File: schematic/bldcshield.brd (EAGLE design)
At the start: 90.2 x 53.3 mm, 51 parts, among them IC1 IR2101SMD, IC2 IR2101SMD, IC3 IR2101SMD, Q3 Shield

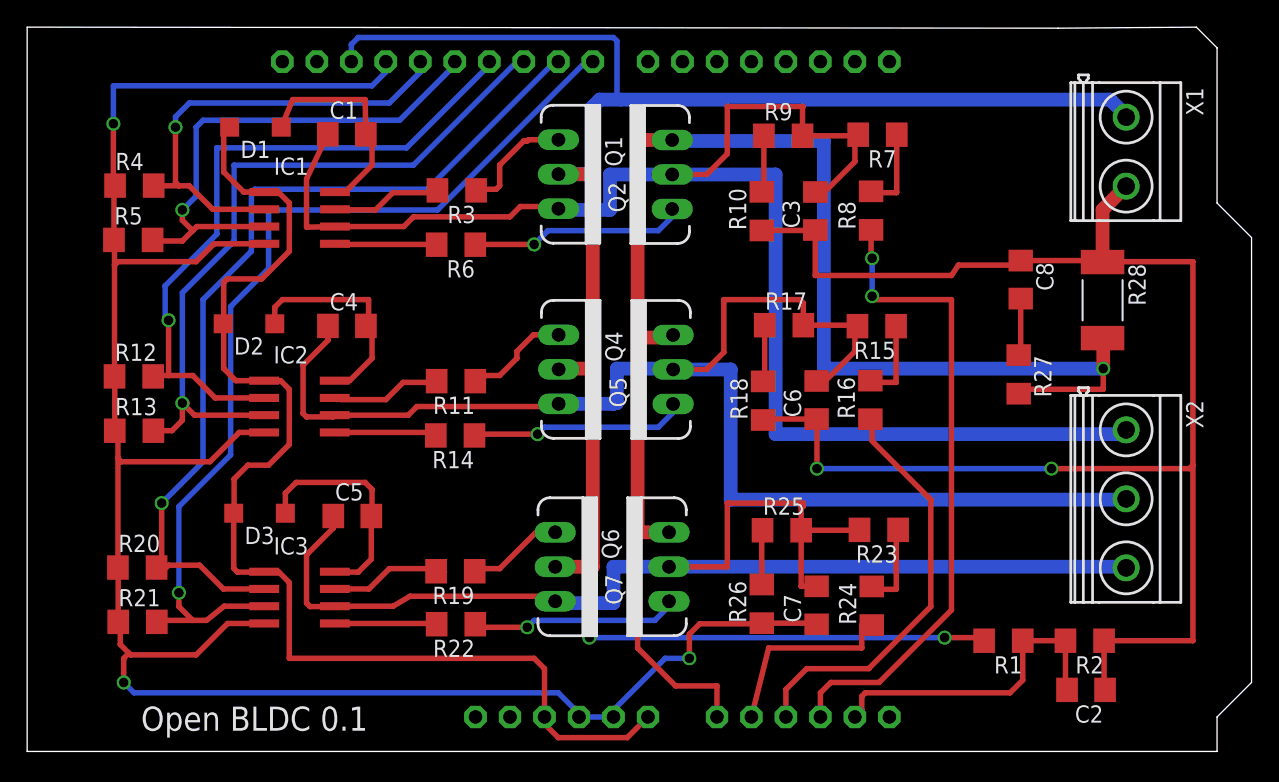
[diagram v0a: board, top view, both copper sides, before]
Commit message: Finalized layout
removed .7z changed to .zip submitted new boards with ground pours to
dirty pcbs.
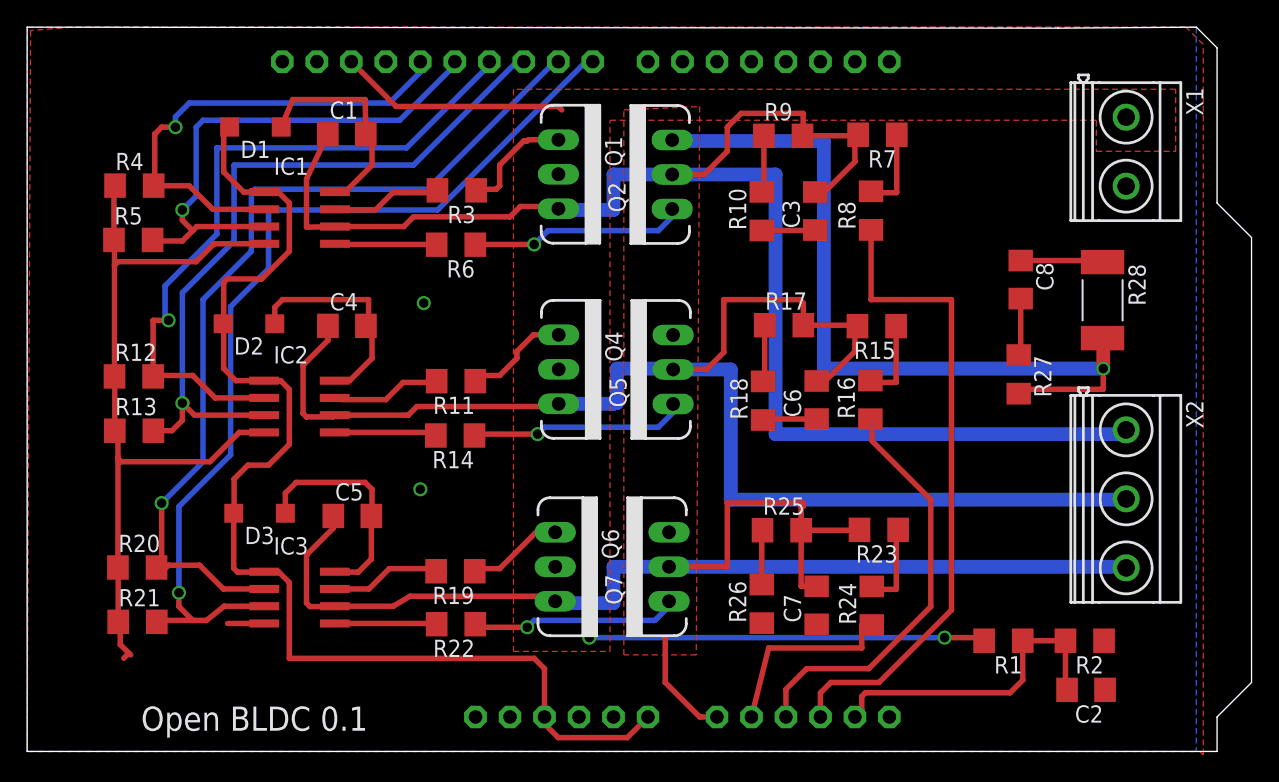
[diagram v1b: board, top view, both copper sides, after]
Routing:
- net GND: track 273.4 -> 77.0 mm, vias 5 -> 2
- net VCC: track 144.6 -> 46.3 mm
- net CURRENT: track 113.2 -> 66.9 mm
- net BLDC1: track 117.0 -> 115.3 mm
- net LO_2: track 50.2 -> 51.4 mm
- net LO_1: track 34.2 -> 35.4 mm
- net EMF1: vias 2 -> 0
- added copper zone on layer 1, net CURRENT
- added copper zone on layer 1, net GND
- added copper zone on layer 16, net GND
- added copper zone on layer 1, net VCC

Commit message: Changed some labels on the sch
I think the finally routed pcb has never been committed.
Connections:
- net HI_1: now also IC1.2, Q3.D13, R4.2; no longer IC1.3, Q3.D12, R5.2
- net HI_2: now also IC2.2, Q3.D11, R12.2; no longer IC2.3, Q3.D10, R13.2
- net HI_3: now also IC3.2, Q3.D9, R20.2; no longer IC3.3, Q3.D8, R21.2
- net LO_1: now also IC1.3, Q3.D12, R5.2; no longer IC1.2, Q3.D13, R4.2
- net LO_2: now also IC2.3, Q3.D10, R13.2; no longer IC2.2, Q3.D11, R12.2
- net LO_3: now also IC3.3, Q3.D8, R21.2; no longer IC3.2, Q3.D9, R20.2
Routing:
- net LO_3: track 65.2 -> 70.1 mm
- net HI_3: track 70.1 -> 65.2 mm
- net LO_1: track 35.4 -> 38.3 mm
- net HI_1: track 38.3 -> 35.4 mm
- net LO_2: track 51.4 -> 54.1 mm
- net HI_2: track 54.1 -> 51.4 mm
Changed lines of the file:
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@@
 <wire x1="89.408" y1="29.718" x2="88.9" y2="29.21" width="0.4064" layer="1"/>
 </signal>
-<signal name="LO_1">
+<signal name="HI_1">
 <contactref element="IC1" pad="2"/>
 <contactref element="R4" pad="2"/>
@@
 <wire x1="37.338" y1="68.4208" x2="37.2574" y2="68.3402" width="0.4064" layer="1"/>
 </signal>
-<signal name="HI_1">
+<signal name="LO_1">
 <contactref element="R5" pad="2"/>
 <contactref element="IC1" pad="3"/>
@@
 <wire x1="39.37" y1="65.786" x2="40.132" y2="65.024" width="0.4064" layer="1"/>
 </signal>
-<signal name="LO_2">
+<signal name="HI_2">
 <contactref element="IC2" pad="2"/>
 <contactref element="R12" pad="2"/>
@@
 <wire x1="37.2174" y1="58.42" x2="37.2174" y2="54.2902" width="0.4064" layer="1"/>
 </signal>
-<signal name="HI_2">
+<signal name="LO_2">
 <contactref element="R13" pad="2"/>
 <contactref element="IC2" pad="3"/>
@@
 <wire x1="37.2392" y1="50.292" x2="37.2374" y2="50.2902" width="0.4064" layer="1"/>
 </signal>
-<signal name="LO_3">
+<signal name="HI_3">
 <contactref element="IC3" pad="2"/>
 <contactref element="R20" pad="2"/>
@@
 <wire x1="37.846" y1="40.59" x2="38.1" y2="40.132" width="0" layer="19" extent="1-1"/>
 </signal>
-<signal name="HI_3">
+<signal name="LO_3">
 <contactref element="R21" pad="2"/>
 <contactref element="IC3" pad="3"/>

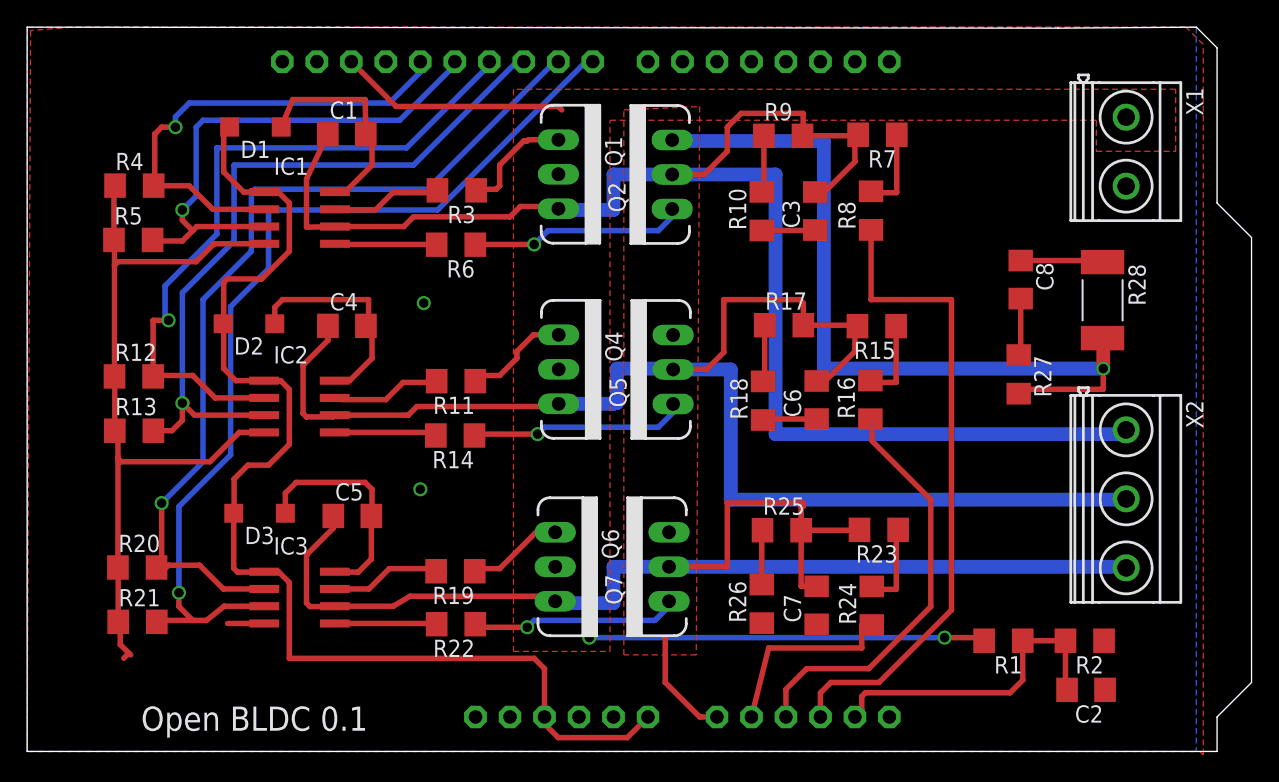
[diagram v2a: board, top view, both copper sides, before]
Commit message: working on arduino micro version schematic
also working on a hall effect code in the BLDC library
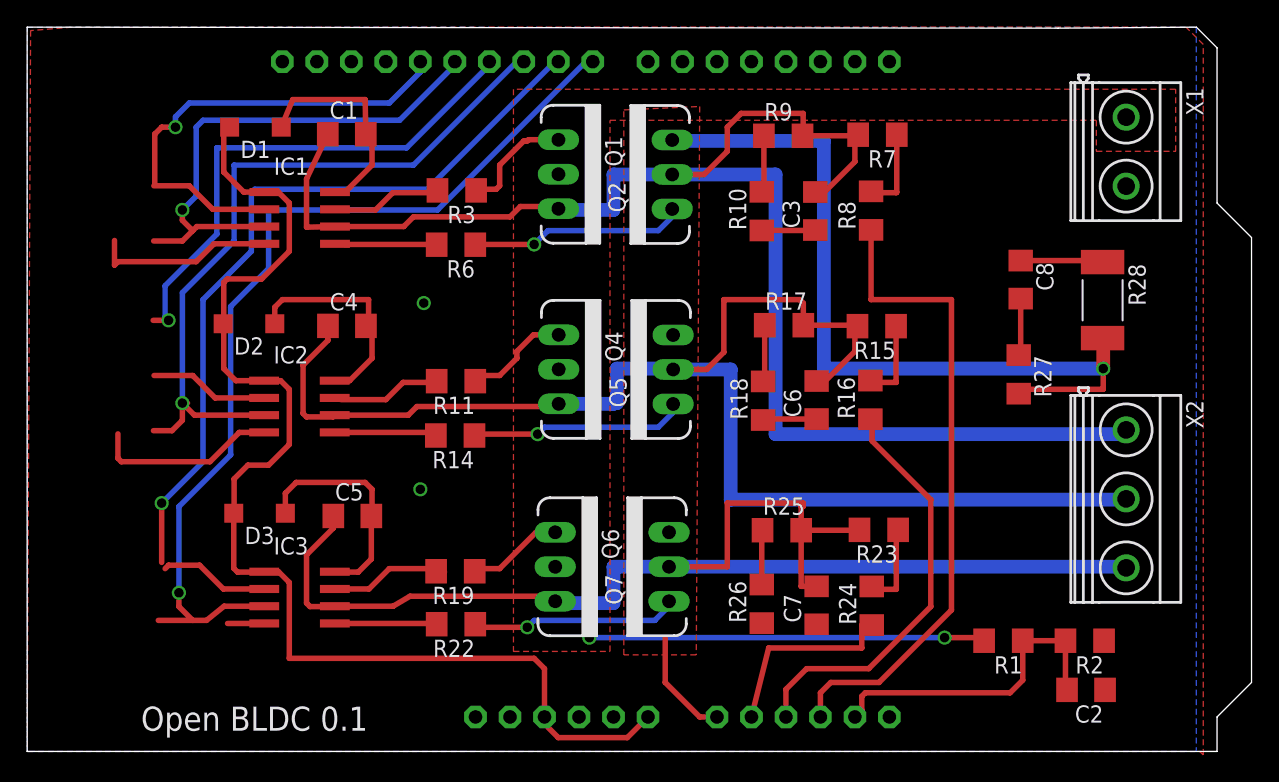
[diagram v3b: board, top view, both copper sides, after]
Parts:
- removed R12, R13, R20, R21, R4, R5: 10k, SmartPrj:R1206
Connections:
- net GND: no longer R12.1, R13.1, R20.1, R21.1, R4.1, R5.1
- net HI_1: no longer R4.2
- net HI_2: no longer R12.2
- net HI_3: no longer R20.2
- net LO_1: no longer R5.2
- net LO_2: no longer R13.2
- net LO_3: no longer R21.2
- net VCC: no longer Q3.AREF
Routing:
- net GND: track 77.0 -> 45.0 mm
- net VCC: track 46.3 -> 29.3 mm
- net HI_2: track 51.4 -> 47.2 mm
- net HI_3: track 65.2 -> 64.7 mm
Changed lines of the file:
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@@
 <layer number="14" name="Route14" color="1" fill="6" visible="no" active="no"/>
 <layer number="15" name="Route15" color="4" fill="6" visible="no" active="no"/>
-<layer number="16" name="Bottom" color="1" fill="1" visible="yes" active="yes"/>
+<layer number="16" name="Bottom" color="1" fill="1" visible="no" active="yes"/>
 <layer number="17" name="Pads" color="2" fill="1" visible="yes" active="yes"/>
 <layer number="18" name="Vias" color="2" fill="1" visible="yes" active="yes"/>
@@
 <element name="C8" library="SmartPrj" package="C1206" value="22p" x="101.11" y="61.42" rot="R270"/>
 <element name="IC3" library="IR" package="SO08" value="IR2101SMD" x="48" y="38" rot="R270"/>
-<element name="R20" library="SmartPrj" package="R1206" value="10k" x="36.048" y="40.214"/>
-<element name="R21" library="SmartPrj" package="R1206" value="10k" x="36.068" y="36.214"/>
 <element name="R22" library="SmartPrj" package="R1206" value="22" x="59.52" y="36.04" rot="R180"/>
 <element name="R19" library="SmartPrj" package="R1206" value="22" x="59.48" y="39.94" rot="R180"/>
@@
 <element name="D3" library="diode" package="SOD123" value="MMSD914" x="45.054" y="44.212" rot="R180"/>
 <element name="IC2" library="IR" package="SO08" value="IR2101SMD" x="47.99" y="52.07" rot="R270"/>
-<element name="R12" library="SmartPrj" package="R1206" value="10k" x="35.7954" y="54.2902"/>
-<element name="R13" library="SmartPrj" package="R1206" value="10k" x="35.8154" y="50.2902"/>
 <element name="R14" library="SmartPrj" package="R1206" value="22" x="59.46" y="49.94" rot="R180"/>
 <element name="R11" library="SmartPrj" package="R1206" value="22" x="59.52" y="53.94" rot="R180"/>
@@
 <element name="D2" library="diode" package="SOD123" value="MMSD914" x="44.276" y="58.166" rot="R180"/>
 <element name="IC1" library="IR" package="SO08" value="IR2101SMD" x="48.01" y="65.96" rot="R270"/>
-<element name="R4" library="SmartPrj" package="R1206" value="10k" x="35.8354" y="68.3402"/>
-<element name="R5" library="SmartPrj" package="R1206" value="10k" x="35.7554" y="64.3402"/>
 <element name="R6" library="SmartPrj" package="R1206" value="22" x="59.52" y="63.99" rot="R180"/>
 <element name="R3" library="SmartPrj" package="R1206" value="22" x="59.58" y="67.99" rot="R180"/>
@@
 <contactref element="R1" pad="2"/>
 <contactref element="X1" pad="1"/>
-<contactref element="Q3" pad="AREF"/>
 <via x="69.342" y="35.052" extent="1-16" drill="0.7"/>
 <wire x1="69.342" y1="35.052" x2="95.504" y2="35.052" width="0.4064" layer="16"/>
@@
 <wire x1="95.504" y1="35.052" x2="98.416" y2="35.052" width="0.4064" layer="1"/>
 <wire x1="98.416" y1="35.052" x2="98.416" y2="34.824" width="0.4064" layer="1"/>
-<wire x1="51.816" y1="77.47" x2="55.118" y2="74.168" width="0.4064" layer="1"/>
-<wire x1="55.118" y1="74.168" x2="67.056" y2="74.168" width="0.4064" layer="1"/>
-<wire x1="67.056" y1="74.168" x2="67.31" y2="73.914" width="0.4064" layer="1"/>
 <polygon width="0.4064" layer="1">
 <vertex x="112.522" y="75.438"/>
@@
 <signal name="HI_1">
 <contactref element="IC1" pad="2"/>
-<contactref element="R4" pad="2"/>
 <contactref element="Q3" pad="D13"/>
 <wire x1="45.41" y1="66.595" x2="41.609" y2="66.595" width="0.4064" layer="1"/>
 <wire x1="41.609" y1="66.595" x2="39.878" y2="68.326" width="0.4064" layer="1"/>
 <wire x1="39.878" y1="68.326" x2="37.2716" y2="68.326" width="0.4064" layer="1"/>
-<wire x1="37.2716" y1="68.326" x2="37.2574" y2="68.3402" width="0.4064" layer="1"/>
 <wire x1="56.896" y1="77.47" x2="56.896" y2="76.708" width="0.4064" layer="16"/>
 <wire x1="56.896" y1="76.708" x2="54.61" y2="74.422" width="0.4064" layer="16"/>
@@
 <wire x1="37.846" y1="72.644" x2="37.338" y2="72.136" width="0.4064" layer="1"/>
 <wire x1="37.338" y1="72.136" x2="37.338" y2="68.4208" width="0.4064" layer="1"/>
-<wire x1="37.338" y1="68.4208" x2="37.2574" y2="68.3402" width="0.4064" layer="1"/>
+<wire x1="37.338" y1="68.4208" x2="37.2716" y2="68.326" width="0" layer="19" extent="1-1"/>
 </signal>
 <signal name="LO_1">
-<contactref element="R5" pad="2"/>
 <contactref element="IC1" pad="3"/>
 <contactref element="Q3" pad="D12"/>
@@
 <wire x1="40.132" y1="65.024" x2="39.37" y2="64.262" width="0.4064" layer="1"/>
 <wire x1="39.37" y1="64.262" x2="37.2556" y2="64.262" width="0.4064" layer="1"/>
-<wire x1="37.2556" y1="64.262" x2="37.1774" y2="64.3402" width="0.4064" layer="1"/>
 <wire x1="59.436" y1="77.47" x2="59.436" y2="77.216" width="0.4064" layer="16"/>
 <wire x1="59.436" y1="77.216" x2="55.372" y2="73.152" width="0.4064" layer="16"/>
@@
 <signal name="HI_2">
 <contactref element="IC2" pad="2"/>
-<contactref element="R12" pad="2"/>
 <contactref element="Q3" pad="D11"/>
 <wire x1="45.39" y1="52.705" x2="41.783" y2="52.705" width="0.4064" layer="1"/>
 <wire x1="41.783" y1="52.705" x2="40.132" y2="54.356" width="0.4064" layer="1"/>
 <wire x1="40.132" y1="54.356" x2="37.2832" y2="54.356" width="0.4064" layer="1"/>
-<wire x1="37.2832" y1="54.356" x2="37.2174" y2="54.2902" width="0.4064" layer="1"/>
 <wire x1="61.976" y1="77.47" x2="61.976" y2="77.216" width="0.4064" layer="16"/>
 <wire x1="61.976" y1="77.216" x2="55.88" y2="71.12" width="0.4064" layer="16"/>
@@
 <via x="38.354" y="58.42" extent="1-16" drill="0.7"/>
 <wire x1="38.354" y1="58.42" x2="37.2174" y2="58.42" width="0.4064" layer="1"/>
-<wire x1="37.2174" y1="58.42" x2="37.2174" y2="54.2902" width="0.4064" layer="1"/>
+<wire x1="37.2832" y1="54.356" x2="37.2174" y2="58.42" width="0" layer="19" extent="1-1"/>
 </signal>
 <signal name="LO_2">
-<contactref element="R13" pad="2"/>
 <contactref element="IC2" pad="3"/>
 <contactref element="Q3" pad="D10"/>
@@
 <wire x1="39.37" y1="51.054" x2="38.608" y2="50.292" width="0.4064" layer="1"/>
 <wire x1="38.608" y1="50.292" x2="37.2392" y2="50.292" width="0.4064" layer="1"/>
-<wire x1="37.2392" y1="50.292" x2="37.2374" y2="50.2902" width="0.4064" layer="1"/>
 </signal>
 <signal name="HI_3">
 <contactref element="IC3" pad="2"/>
-<contactref element="R20" pad="2"/>
 <contactref element="Q3" pad="D9"/>
 <wire x1="45.4" y1="38.635" x2="42.391" y2="38.635" width="0.4064" layer="1"/>
@@
 <via x="37.846" y="44.958" extent="1-16" drill="0.7"/>
 <wire x1="37.846" y1="44.958" x2="37.846" y2="40.59" width="0.4064" layer="1"/>
-<wire x1="37.846" y1="40.59" x2="37.47" y2="40.214" width="0.4064" layer="1"/>
 <wire x1="37.846" y1="40.59" x2="38.1" y2="40.132" width="0" layer="19" extent="1-1"/>
 </signal>
 <signal name="LO_3">
-<contactref element="R21" pad="2"/>
 <contactref element="IC3" pad="3"/>
 <contactref element="Q3" pad="D8"/>
@@
 <wire x1="41.148" y1="36.322" x2="40.132" y2="36.322" width="0.4064" layer="1"/>
 <wire x1="40.132" y1="36.322" x2="37.598" y2="36.322" width="0.4064" layer="1"/>
-<wire x1="37.598" y1="36.322" x2="37.49" y2="36.214" width="0.4064" layer="1"/>
 <wire x1="69.596" y1="77.47" x2="69.088" y2="77.47" width="0.4064" layer="16"/>
 <wire x1="69.088" y1="77.47" x2="58.166" y2="66.548" width="0.4064" layer="16"/>
@@
 <contactref element="Q3" pad="GND2"/>
 <contactref element="R28" pad="1"/>
-<contactref element="R20" pad="1"/>
-<contactref element="R21" pad="1"/>
 <contactref element="IC3" pad="4"/>
-<contactref element="R12" pad="1"/>
-<contactref element="R13" pad="1"/>
 <contactref element="IC2" pad="4"/>
-<contactref element="R4" pad="1"/>
-<contactref element="R5" pad="1"/>
 <contactref element="IC1" pad="4"/>
 <contactref element="C2" pad="1"/>
@@
 <wire x1="107.25" y1="31.276" x2="107.322" y2="31.204" width="0.4064" layer="1"/>
 <wire x1="107.14" y1="62.738" x2="107.14" y2="62.71" width="0.4064" layer="1"/>
-<wire x1="34.646" y1="36.214" x2="34.646" y2="40.194" width="0.4064" layer="1"/>
-<wire x1="34.646" y1="40.194" x2="34.626" y2="40.214" width="0.4064" layer="1"/>
-<wire x1="34.626" y1="40.214" x2="34.626" y2="48.26" width="0.4064" layer="1"/>
 <wire x1="34.626" y1="48.26" x2="34.626" y2="50.0576" width="0.4064" layer="1"/>
-<wire x1="34.626" y1="50.0576" x2="34.3934" y2="50.2902" width="0.4064" layer="1"/>
-<wire x1="34.3934" y1="50.2902" x2="34.3934" y2="54.2702" width="0.4064" layer="1"/>
-<wire x1="34.3934" y1="54.2702" x2="34.3734" y2="54.2902" width="0.4064" layer="1"/>
-<wire x1="34.3734" y1="54.2902" x2="34.3734" y2="62.484" width="0.4064" layer="1"/>
 <wire x1="34.3734" y1="62.484" x2="34.3734" y2="64.3002" width="0.4064" layer="1"/>
-<wire x1="34.3734" y1="64.3002" x2="34.3334" y2="64.3402" width="0.4064" layer="1"/>
-<wire x1="34.3334" y1="64.3402" x2="34.3334" y2="68.2602" width="0.4064" layer="1"/>
-<wire x1="34.3334" y1="68.2602" x2="34.4134" y2="68.3402" width="0.4064" layer="1"/>
 <wire x1="45.41" y1="64.055" x2="41.703" y2="64.055" width="0.4064" layer="1"/>
 <wire x1="41.703" y1="64.055" x2="40.386" y2="62.738" width="0.4064" layer="1"/>
@@
 <wire x1="34.88" y1="48.006" x2="34.626" y2="48.26" width="0.4064" layer="1"/>
 <wire x1="45.4" y1="36.095" x2="42.699" y2="36.095" width="0.4064" layer="1"/>
-<wire x1="35.56" y1="33.782" x2="35.433" y2="33.909" width="0.4064" layer="1"/>
-<wire x1="35.433" y1="33.909" x2="34.798" y2="34.544" width="0.4064" layer="1"/>
-<wire x1="34.798" y1="34.544" x2="34.798" y2="36.062" width="0.4064" layer="1"/>
-<wire x1="34.798" y1="36.062" x2="34.646" y2="36.214" width="0.4064" layer="1"/>
 <wire x1="68.58" y1="29.21" x2="68.58" y2="29.464" width="0.4064" layer="16"/>
-<wire x1="35.052" y1="33.528" x2="35.433" y2="33.909" width="0.4064" layer="1"/>
 <polygon width="0.4064" layer="1" rank="3">
 <vertex x="28.194" y="79.756"/>
